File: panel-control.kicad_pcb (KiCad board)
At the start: 4 copper layers, 65 x 45 mm, 57 parts, among them J1 POWER_CONN, J2 SWIM, J3 PWR, J4 40HAT, J5 HUB-75_A, J6 HUB-75_B, J7 VBAT, J8 FAN, J9 MK_R, Q3 AO4407A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

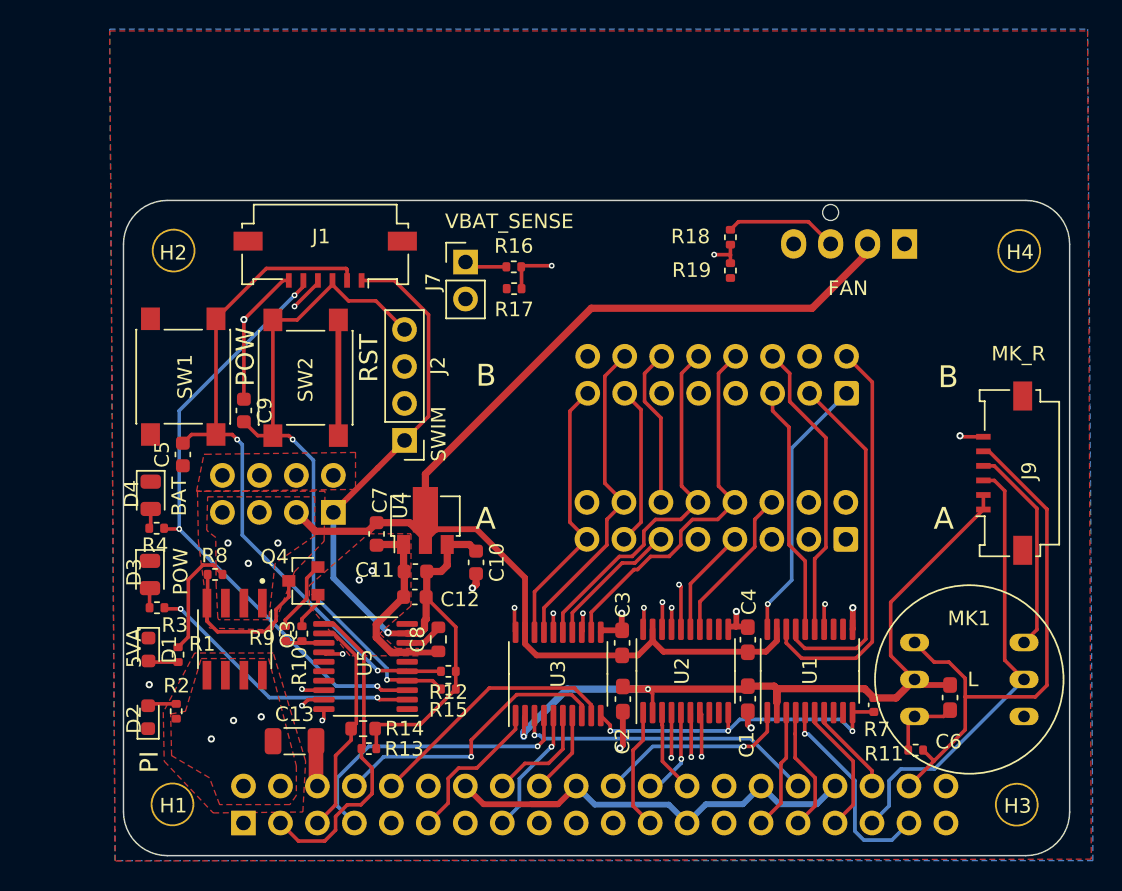
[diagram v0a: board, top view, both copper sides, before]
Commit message: maybe finished revision with micro usb output
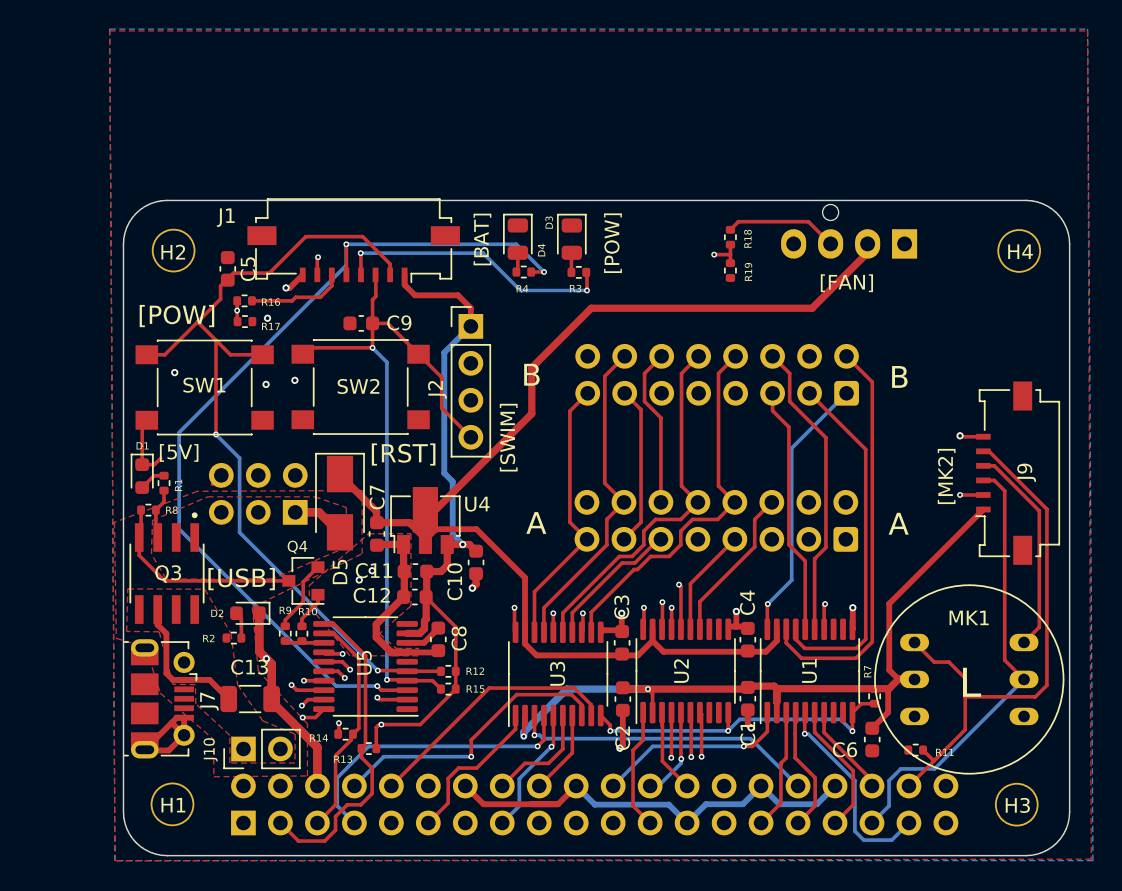
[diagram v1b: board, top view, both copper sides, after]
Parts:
- added D5: D, Diode_SMD:D_SMA, F.Cu at (93.5, 43.6)
- added J10: PWR_HAT, Connector_PinHeader_2.54mm:PinHeader_1x02_P2.54mm_Vertical, F.Cu at (86.9, 60.5)
- C1, C2, C3, C4, C6: footprint Capacitor_SMD:C_0603_1608Metric_Pad1.08x0.95mm_HandSolder -> Capacitor_SMD:C_0603_1608Metric
- C13: value 1uf -> 10uf
- C8: footprint Resistor_SMD:R_0603_1608Metric -> Capacitor_SMD:C_0603_1608Metric
- J1: footprint Connector_FFC-FPC:Molex_200528-0060_1x06-1MP_P1.00mm_Horizontal -> Connector_FFC-FPC:Molex_200528-0080_1x08-1MP_P1.00mm_Horizontal
- J3: footprint Connector_PinHeader_2.54mm:PinHeader_2x04_P2.54mm_Vertical -> Connector_PinHeader_2.54mm:PinHeader_2x03_P2.54mm_Vertical
- J7: value VBAT -> USB_PWR; footprint Connector_PinHeader_2.54mm:PinHeader_1x02_P2.54mm_Vertical -> Connector_USB:USB_Micro-B_Molex-105017-0001
- J9: value MK_R -> I2S
- R14: footprint Resistor_SMD:R_0603_1608Metric -> Resistor_SMD:R_0402_1005Metric
- R7: footprint Capacitor_SMD:C_0402_1005Metric -> Resistor_SMD:R_0402_1005Metric
- moved D3 37.0 mm to (109.5, 25.5)
- moved R3 37.0 mm to (110.0, 27.8)
- moved J7 36.5 mm to (81.4, 57.1), turned to 270 degrees
- moved R4 30.8 mm to (106.2, 27.7)
- moved D4 30.8 mm to (105.8, 25.5)
- moved R16 18.6 mm to (87.0, 29.7), turned to 180 degrees
- moved R17 18.6 mm to (87.0, 31.1), turned to 0 degrees
- moved C5 13.1 mm to (85.8, 27.5), turned to 270 degrees
- moved D1 11.9 mm to (80.0, 41.8)
- moved R1 11.8 mm to (81.5, 42.2), turned to 90 degrees
- moved C9 10.0 mm to (95.0, 31.3), turned to 0 degrees
- moved D2 9.90 mm to (87.2, 51.2), turned to 180 degrees
- moved J2 9.07 mm to (102.5, 31.5), turned to 0 degrees
- moved Q3 6.48 mm to (81.7, 48.4)
- moved R2 6.41 mm to (86.3, 52.9), turned to 0 degrees
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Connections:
- C13 pad 1: /P5V_HAT -> +5VP
- J1 pad 6: GND -> /VBAT_SENSE
- J3 pad 1: +3V3 -> +5V
- J3 pad 3: +5VA -> +5V
- J3 pad 5: +5VA -> +5V
- J4 pad 27: /ID_SD_EEPROM -> /GPIO_SHUTDOWN
- J4 pad 28: /ID_SC_EEPROM -> /GPIO_POWEROFF
- J7 pad 1: /VBAT_SENSE -> +5VP
- J7 pad 2: GND -> Net-(J7-Pad2)
- J9 pad 2: +3.3VA -> /I2S_OUT
- Q3 pad 1: +5VA -> +5V
- Q3 pad 2: +5VA -> +5V
- Q3 pad 3: +5VA -> +5V
- Q3 pad 5: /P5V_HAT -> +5VP
- Q3 pad 6: /P5V_HAT -> +5VP
- Q3 pad 7: /P5V_HAT -> +5VP
- Q3 pad 8: /P5V_HAT -> +5VP
- R1 pad 1: +5VA -> +5V
- R2 pad 1: /P5V_HAT -> +5VP
- R8 pad 2: +5VA -> +5V
- U5 pad 15: Net-(U5-Pad15) -> /GPIO_SHUTDOWN
- U5 pad 16: Net-(U5-Pad16) -> /GPIO_POWEROFF
- U5 pad 17: Net-(U5-Pad17) -> /EXT_POWER
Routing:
- net /GPIO_SHUTDOWN: track 0.00 -> 40.4 mm, vias 0 -> 1
- net /GPIO_POWEROFF: track 0.00 -> 35.7 mm, vias 0 -> 1
- net /EXT_POWER: track 0.00 -> 32.1 mm, vias 0 -> 2
- net /LED_PWR: track 45.8 -> 69.2 mm
- net /I2S_OUT: track 0.00 -> 22.0 mm, vias 0 -> 1
- net /LED_BAT: track 41.9 -> 61.9 mm
- net /BUT_POW: track 47.5 -> 59.2 mm
- net +5VA: track 94.6 -> 83.8 mm, vias 3 -> 0
- net Net-(R16-Pad2): track 42.7 -> 32.6 mm
- net +5VP: track 0.00 -> 9.65 mm
- net +5V: track 0.00 -> 7.32 mm
- net /SWIM: track 24.1 -> 30.6 mm
- net +3V3: track 58.8 -> 52.9 mm, vias 1 -> 3
- net GND: track 107.9 -> 112.5 mm, vias 11 -> 15
- net /FAN_PWM: track 51.9 -> 47.6 mm
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- added copper zone on F.Cu, net +5V
- added copper zone on F.Cu, net +5VP
- removed copper zone on F.Cu, net +5VA
- removed copper zone on In2.Cu, net +5VA
- removed copper zone on F.Cu, net /P5V_HAT
- removed copper zone on In2.Cu, net /P5V_HAT
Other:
- board text added: "[5V]"
- board text added: "[BAT]"
- board text added: "[FAN]"
- board text added: "[MK2]"
- board text added: "[POW]"
- board text added: "[RST]"
- board text added: "[SWIM]"
- board text added: "[USB]"
- board text removed: "5VA"
- board text removed: "BAT"
- board text removed: "FAN"
- board text removed: "MK_R"
- board text removed: "PI"
- board text removed: "POW"
- board text removed: "RST"
- board text removed: "SWIM"
- board text removed: "VBAT_SENSE"

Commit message: better reverse current protection and usb-c power
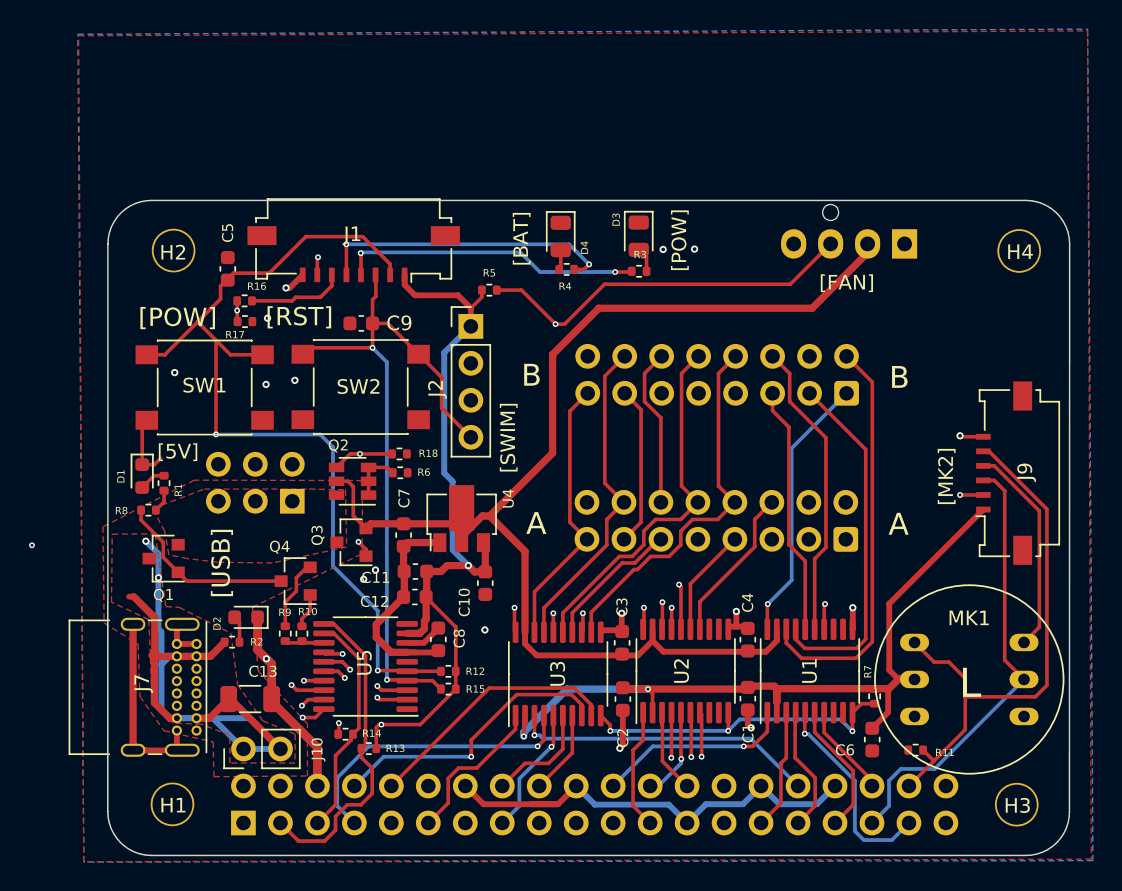
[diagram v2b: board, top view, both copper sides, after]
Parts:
- removed D5: D, Diode_SMD:D_SMA
- removed R19: 10k, Resistor_SMD:R_0402_1005Metric
- added Q1: DMG2305UX, Package_TO_SOT_SMD:SOT-23, F.Cu at (81.4, 47.4)
- added Q2: DMMT5401, Package_TO_SOT_SMD:SOT-23-6, F.Cu at (94.4, 42.1)
- added R5: 4.7k, Resistor_SMD:R_0402_1005Metric, F.Cu at (103.8, 29.0)
- added R6: 10k, Resistor_SMD:R_0402_1005Metric, F.Cu at (97.7, 41.5)
- J7: footprint Connector_USB:USB_Micro-B_Molex-105017-0001 -> Connector_USB:USB_C_Receptacle_GCT_USB4085
- Q3: value AO4407A -> DMG2305UX; footprint libraries:SOIC127P600X175-8N -> Package_TO_SOT_SMD:SOT-23
- R18: value 10k -> 47k
- moved R18 27.2 mm to (97.6, 40.2), turned to 0 degrees
- moved Q3 12.9 mm to (94.3, 46.3), turned to 180 degrees
- moved D3 4.60 mm to (114.1, 25.3)
- moved J7 4.42 mm to (83.7, 53.3)
- moved R3 4.14 mm to (114.1, 27.7), turned to 0 degrees
- moved D4 2.95 mm to (108.7, 25.3)
- moved R4 2.95 mm to (109.1, 27.6)
- moved U4 2.49 mm to (101.9, 44.7)
- moved C7 1.83 mm to (97.9, 45.8)
- moved C10 1.56 mm to (103.5, 49.1)
- moved J3 0.79 mm to (90.3, 43.5)
- moved Q4 0.53 mm to (90.5, 49.0)
- moved D2 0.31 mm to (87.1, 51.5)
- moved R2 0.31 mm to (86.1, 53.2)
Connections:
- Q3 pad 1: +5V -> Net-(Q2-Pad4)
- Q3 pad 2: +5V -> +5VA
- Q4 pad 3: Net-(Q3-Pad4) -> Net-(Q1-Pad1)
- R18 pad 1: /FAN_TACH -> Net-(Q2-Pad4)
- R18 pad 2: Net-(R18-Pad2) -> GND
- R8 pad 1: Net-(Q3-Pad4) -> Net-(Q1-Pad1)
- U5 pad 20: Net-(R18-Pad2) -> /FAN_TACH
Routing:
- net +5VP: track 9.65 -> 97.7 mm, vias 0 -> 2
- net /FAN_TACH: track 7.82 -> 62.1 mm, vias 0 -> 2
- net Net-(R18-Pad2): track 51.1 -> 0.00 mm, vias 2 -> 0
- net GND: track 112.5 -> 128.9 mm, vias 15 -> 17
- net /LED_PWR: track 69.2 -> 55.0 mm
- net Net-(Q3-Pad4): track 14.2 -> 0.00 mm
- net Net-(Q1-Pad1): track 0.00 -> 12.7 mm
- net Net-(Q2-Pad4): track 0.00 -> 11.5 mm, vias 0 -> 2
- net /LED_BAT: track 61.9 -> 54.0 mm
- net +5V: track 7.32 -> 1.58 mm
- net +3V3: track 52.9 -> 57.3 mm
- net /BUT_POW: track 59.2 -> 63.4 mm
- net Net-(Q2-Pad1): track 0.00 -> 3.72 mm
- net /FAN_PWM: track 47.6 -> 49.2 mm
- net +5VA: track 83.8 -> 82.9 mm
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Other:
- board size 65 x 45 mm -> 66.1 x 45 mm

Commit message: more revisions, maybe ready to submit
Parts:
- removed C8: 1uF, Capacitor_SMD:C_0603_1608Metric
- removed U5: STM8S103F3P, Package_SO:TSSOP-20_4.4x6.5mm_P0.65mm
- added J11: BOOT, Connector_PinHeader_2.54mm:PinHeader_1x02_P2.54mm_Vertical, F.Cu at (138.8, 32.0)
- added R19: 4.7k, Resistor_SMD:R_0402_1005Metric, F.Cu at (135.2, 29.6)
- added R20: 47k, Resistor_SMD:R_0402_1005Metric, F.Cu at (135.3, 33.2)
- added U7: STM32L031F6Px, Package_SO:TSSOP-20_4.4x6.5mm_P0.65mm, F.Cu at (96.0, 54.7)
- C10, C7: value 1uF -> 10uf
- C13: footprint Capacitor_SMD:C_1206_3216Metric -> Capacitor_SMD:C_0603_1608Metric
- J2: value SWIM -> PROG; footprint Connector_PinHeader_2.54mm:PinHeader_1x04_P2.54mm_Vertical -> Connector_PinHeader_2.54mm:PinHeader_1x06_P2.54mm_Vertical
- R1, R2, R3, R4: value 330 -> 470
- R12, R15: value 4.7k -> 47k
- R13, R14: value 4.7k -> 470
- R7: value 4.7K -> 4.7k
- moved R13 29.5 mm to (104.9, 32.5), turned to 90 degrees
- moved R14 26.8 mm to (104.8, 35.0), turned to 90 degrees
- moved R15 25.0 mm to (99.3, 31.4)
- moved R12 24.9 mm to (99.3, 30.3)
- moved C12 5.61 mm to (101.3, 55.0), turned to 90 degrees
- moved C11 5.46 mm to (102.1, 52.6), turned to 180 degrees
- moved U4 4.56 mm to (98.9, 48.1)
- moved C7 1.75 mm to (97.7, 44.1), turned to 90 degrees
- moved R5 1.25 mm to (103.9, 27.7)
- moved C10 1.09 mm to (102.4, 49.1), turned to 90 degrees
- moved J2 0.56 mm to (102.4, 30.9)
- moved C13 0.51 mm to (87.8, 57.3)
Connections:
- C9 pad 2: /NRST -> /CTS
- J1 pad 3: /NRST -> /CTS
- J2 pad 1: +3V3 -> /BOOT
- J2 pad 2: /SWIM -> Net-(J2-Pad2)
- J2 pad 3: GND -> Net-(J2-Pad3)
- J2 pad 4: /NRST -> +3V3
- R13 pad 1: +3V3 -> Net-(J2-Pad2)
- R13 pad 2: /I2C_SDA -> /USART_RX
- R14 pad 1: +3V3 -> Net-(J2-Pad3)
- R14 pad 2: /I2C_SCL -> /USART_TX
- R15 pad 2: /NRST -> /CTS
- SW2 pad 1: /NRST -> /CTS
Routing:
- net /BOOT: track 0.00 -> 79.8 mm, vias 0 -> 2
- net /CTS: track 0.00 -> 49.6 mm, vias 0 -> 2
- net /NRST: track 48.5 -> 0.00 mm, vias 2 -> 0
- net +3V3: track 57.3 -> 96.9 mm, vias 3 -> 4
- net /USART_RX: track 0.00 -> 34.9 mm, vias 0 -> 2
- net /USART_TX: track 0.00 -> 31.1 mm, vias 0 -> 2
- net /SWIM: track 30.6 -> 0.00 mm, vias 1 -> 0
- net GND: track 128.9 -> 119.1 mm, vias 17 -> 19
- net +5VP: track 97.7 -> 105.6 mm
- net Net-(R16-Pad2): track 32.8 -> 39.6 mm
- net +5VA: track 82.9 -> 89.4 mm
- net /FAN_PWM: track 49.2 -> 55.2 mm
- net +5V: track 1.58 -> 6.89 mm, vias 0 -> 1
- net /LED_BAT: track 54.0 -> 49.6 mm
- net Net-(J11-Pad1): track 0.00 -> 4.32 mm
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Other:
- board text added: "Steven Cohen 01-10-2021 Vuzic Panel Adapter v0.1 peragwin@gmail.com"
- board text added: "[PROG]"
- board text removed: "[SWIM]"

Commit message: tweak
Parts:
- added G***: LOGO, libraries:peragato, B.Cu at (95.7, 50.9)
- moved R11 12.6 mm to (134.8, 48.1)
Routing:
- net /M_SD: track 38.6 -> 26.3 mm
- net +3.3VA: track 92.4 -> 91.3 mm
- net /M_SCK: track 59.6 -> 58.7 mm

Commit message: finally submitted
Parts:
- removed C2: 100nF, Capacitor_SMD:C_0603_1608Metric
- added R21: 4.7k, Resistor_SMD:R_0402_1005Metric, F.Cu at (104.9, 59.5)
- added R22: 4.7k, Resistor_SMD:R_0402_1005Metric, F.Cu at (113.8, 50.7)
- added R23: 4.7k, Resistor_SMD:R_0402_1005Metric, F.Cu at (122.9, 50.5)
- U1, U2, U3: value TXS0108EPW -> 74HC245; footprint Package_SO:TSSOP-20_4.4x6.5mm_P0.65mm -> Package_SO:SSOP-20_4.4x6.5mm_P0.65mm
- moved R7 25.4 mm to (106.2, 48.9), turned to 180 degrees
- moved C1 17.6 mm to (104.1, 55.1)
- moved U3 17.4 mm to (125.9, 55.0)
- moved U1 17.3 mm to (108.6, 55.1)
- moved R8 8.55 mm to (88.1, 47.9), turned to 90 degrees
- moved D2 8.15 mm to (80.8, 46.3), turned to 270 degrees
- moved R2 5.69 mm to (82.4, 48.8), turned to 180 degrees
- moved Q1 4.18 mm to (85.5, 48.5)
- moved D4 3.12 mm to (111.8, 25.7), turned to 0 degrees
- moved D3 2.92 mm to (117.0, 25.6), turned to 180 degrees
- moved R4 2.87 mm to (112.0, 27.5), turned to 0 degrees
- moved R3 1.75 mm to (115.8, 27.4)
- moved R1 1.35 mm to (82.4, 43.2)
- moved D1 0.87 mm to (80.8, 41.9)
- moved C6 0.84 mm to (130.7, 60.4), turned to 180 degrees
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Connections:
- C1 pad 1: +3.3VA -> +5VA
- R7 pad 1: +3.3VA -> /LS_OE
- R7 pad 2: /LS_OE -> +5VA
- U1 pad 1: /R1B_A -> /LS_DIR
- U1 pad 10: /LS_OE -> GND
- U1 pad 11: GND -> /E_B
- U1 pad 12: Net-(U1-Pad12) -> /D_B
- U1 pad 13: Net-(U1-Pad13) -> /C_B
- U1 pad 14: /B2B_B -> /B_B
- U1 pad 15: /G2B_B -> /A_B
- U1 pad 16: /R2B_B -> /STB_B
- U1 pad 17: /B1B_B -> /OE_B
- U1 pad 18: /G1B_B -> /CLK_B
- U1 pad 19: +5VA -> /LS_OE
- U1 pad 2: +3.3VA -> /CLK_A
- U1 pad 20: /R1B_B -> +5VA
- U1 pad 3: /G1B_A -> /OE_A
- U1 pad 4: /B1B_A -> /STB_A
- U1 pad 5: /R2B_A -> /A_A
- U1 pad 6: /G2B_A -> /B_A
- U1 pad 7: /B2B_A -> /C_A
- U1 pad 8: Net-(U1-Pad8) -> /D_A
- U1 pad 9: Net-(U1-Pad9) -> /E_A
- U2 pad 1: /R1A_A -> /LS_DIR
- U2 pad 10: /LS_OE -> GND
- U2 pad 11: GND -> Net-(U2-Pad11)
- U2 pad 13: Net-(U2-Pad13) -> /G2A_B
- U2 pad 14: /G2A_B -> /B2A_B
- U2 pad 15: /B2A_B -> /R2A_B
- U2 pad 16: /R2A_B -> /G1A_B
- U2 pad 17: /G1A_B -> /B1A_B
- U2 pad 18: /B1A_B -> /R1A_B
- U2 pad 19: +5VA -> Net-(R22-Pad1)
- U2 pad 2: +3.3VA -> /R1A_A
- U2 pad 20: /R1A_B -> +5VA
- U3 pad 1: /CLK_A -> /LS_DIR
- U3 pad 10: /LS_OE -> GND
- U3 pad 11: GND -> Net-(U3-Pad11)
- U3 pad 12: /E_B -> Net-(U3-Pad12)
- U3 pad 13: /D_B -> /B2B_B
- U3 pad 14: /C_B -> /G2B_B
- U3 pad 15: /B_B -> /R2B_B
- U3 pad 16: /A_B -> /B1B_B
- U3 pad 17: /STB_B -> /G1B_B
- U3 pad 18: /OE_B -> /R1B_B
- U3 pad 19: +5VA -> Net-(R23-Pad1)
- U3 pad 2: +3.3VA -> /R1B_A
- U3 pad 20: /CLK_B -> +5VA
- U3 pad 3: /OE_A -> /G1B_A
- U3 pad 4: /STB_A -> /B1B_A
- U3 pad 5: /A_A -> /R2B_A
- U3 pad 6: /B_A -> /G2B_A
- U3 pad 7: /C_A -> /B2B_A
- U3 pad 8: /D_A -> Net-(U3-Pad8)
- U3 pad 9: /E_A -> Net-(U3-Pad9)
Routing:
- net /LS_DIR: track 0.00 -> 23.5 mm, vias 0 -> 2
- net /LS_OE: track 22.9 -> 3.44 mm, vias 3 -> 0
- net GND: track 119.1 -> 102.5 mm, vias 19 -> 14
- net +5VA: track 89.4 -> 102.6 mm, vias 0 -> 2
- net Net-(Q1-Pad1): track 12.7 -> 3.73 mm
- net +3.3VA: track 91.3 -> 83.1 mm, vias 2 -> 0
- net +5V: track 6.89 -> 13.6 mm
- net /B2B_B: track 19.0 -> 22.6 mm
- net /R1B_B: track 18.5 -> 21.7 mm
- net +5VP: track 105.6 -> 108.5 mm
- net /M_SCK: track 58.7 -> 60.9 mm
- net /G2B_B: track 20.6 -> 22.4 mm
- net Net-(R22-Pad1): track 0.00 -> 1.73 mm
- net Net-(R23-Pad1): track 0.00 -> 1.73 mm
- net /CLK_A: track 10.6 -> 12.2 mm
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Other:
- net class Default: via_dia 0.4 -> 0.5; via_drill 0.2 -> 0.3
- rule pad_to_mask_clearance: 0.1 -> 0.15
- rule via_min_drill: 0.2 -> 0.3
- rule via_min_size: 0.4 -> 0.5
- board text added: "+5V"
- board text added: "GND"
- board text added: "[CONN]"
- board text removed: "POWER_FPC"
